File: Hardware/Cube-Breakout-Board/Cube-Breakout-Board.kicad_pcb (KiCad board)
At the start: 2 copper layers, 4 parts, among them J1 Conn_01x22, J2 Conn_01x30, J3 Pixhawk_Cube_DF17_80_Pin_Grou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, J4 Conn_01x30

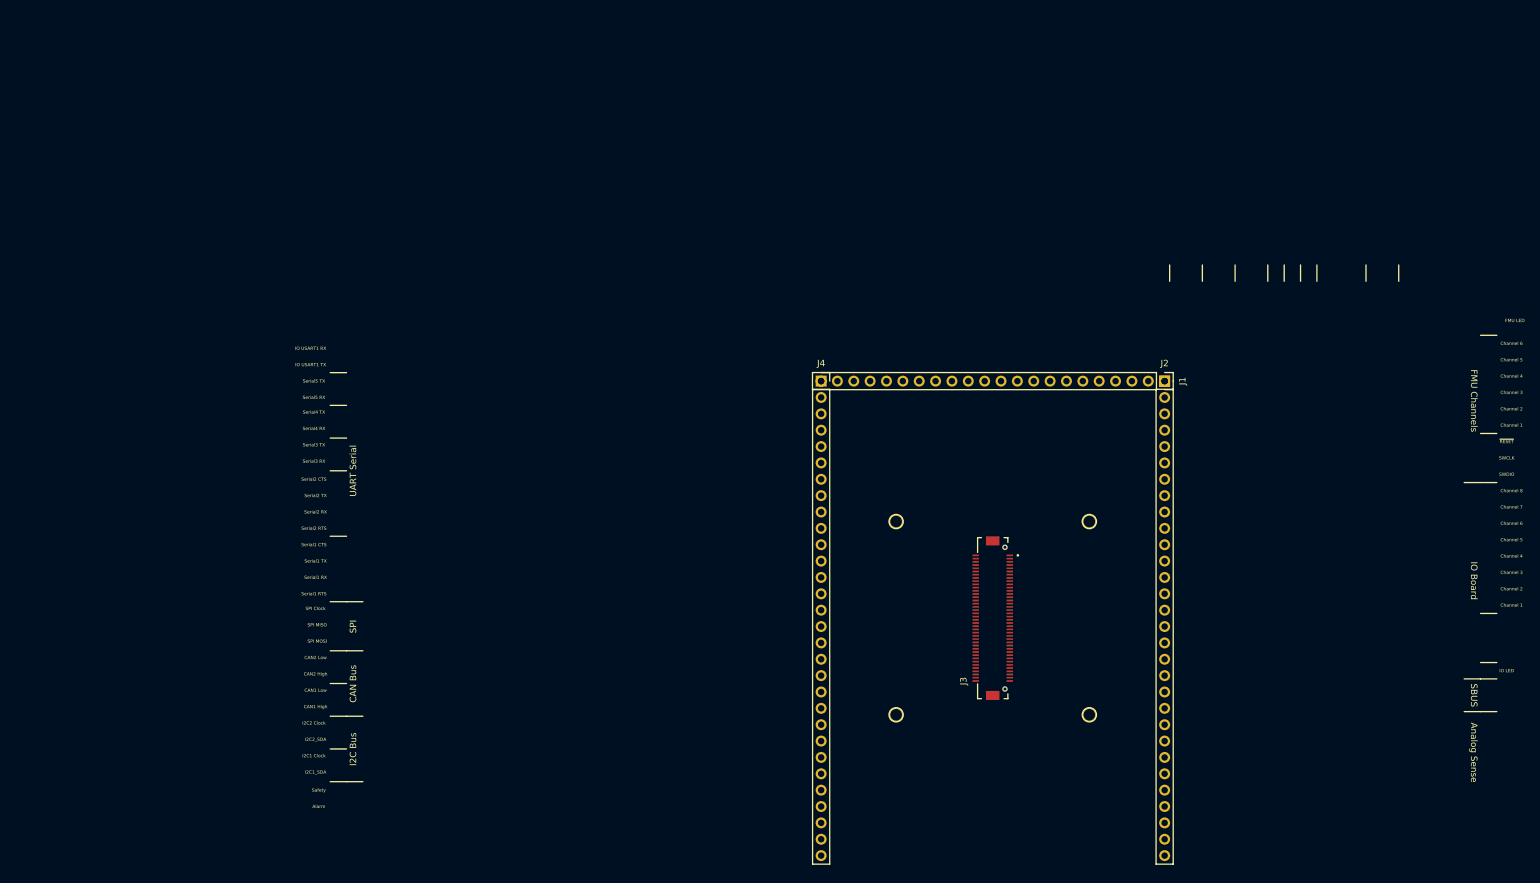
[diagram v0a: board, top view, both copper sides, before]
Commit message: Finished routing, board sizing, silkscreen text
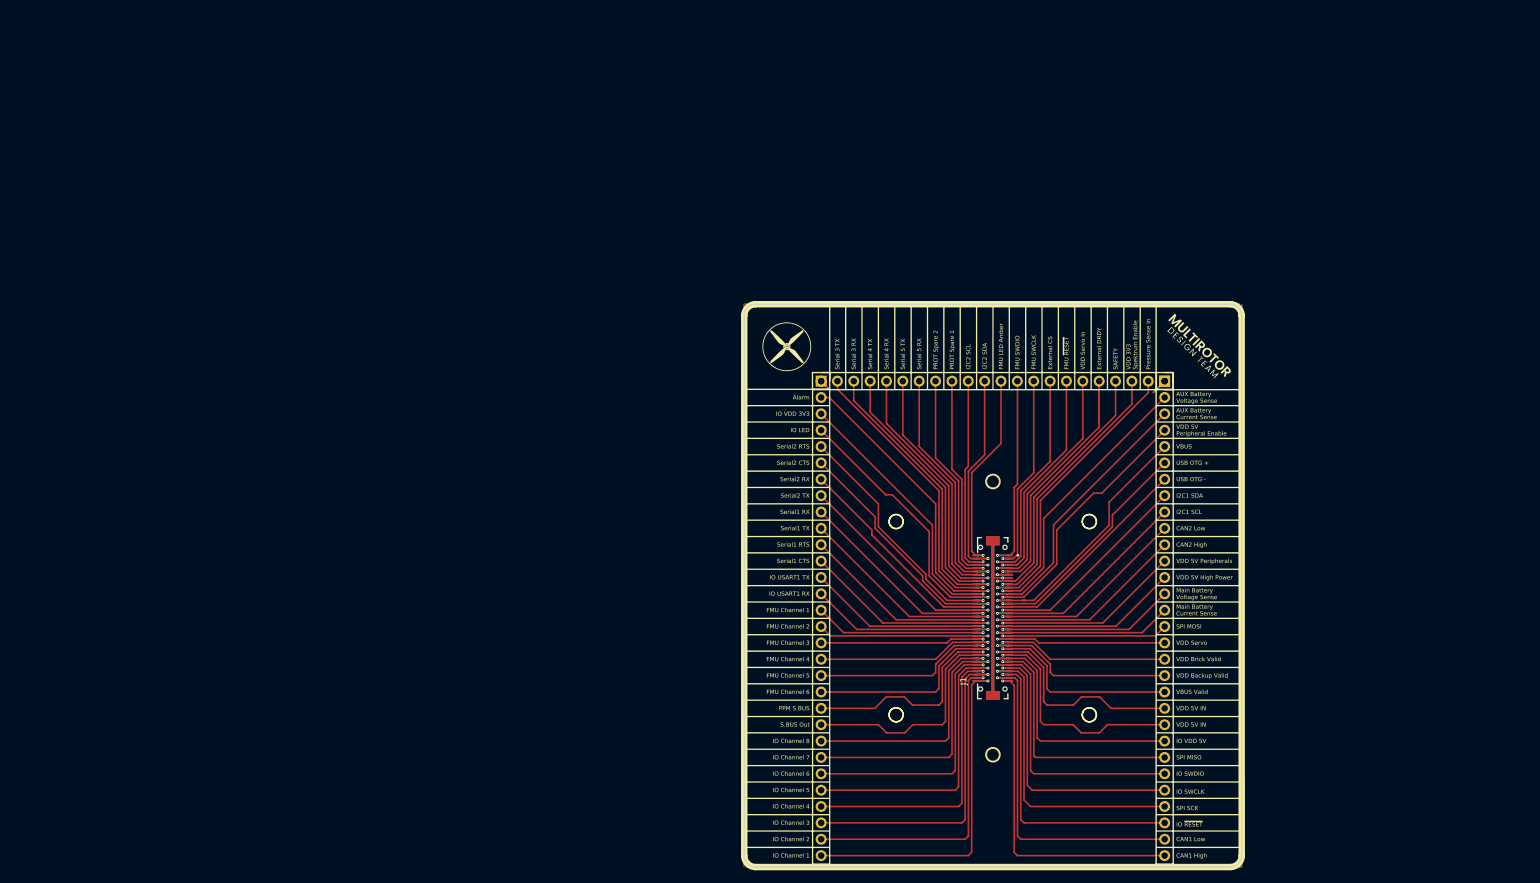
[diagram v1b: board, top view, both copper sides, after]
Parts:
- added ?: , clipboard:d1fccd29-87df-4368-b673-df9ed64eb982, F.Cu at (207.0, 132.8)
- added ?: , clipboard:d1fccd29-87df-4368-b673-df9ed64eb982, F.Cu at (207.0, 90.4)
- added G***: LOGO, libraries:MRR Logo Text, F.Cu at (238.7, 70.9)
- added G***: LOGO, libraries:MRR Logo 1, F.Cu at (175.0, 71.8)
- added J2: Pixhawk_Cube_DF17_80_Pin_Grouped, libraries:Cube_DF17_Mount, B.Cu at (207.0, 112.7)
- renumbered J3 to J1, J4 to J3, J1 to J4, J2 to J5
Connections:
- J1 pad 81: (no net) -> GND
- J1 pad S1: (no net) -> GND
- J1 pad S2: (no net) -> GND
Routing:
- net /VDD_5V_IN_PROT: track 0.00 -> 72.2 mm, vias 0 -> 2
- net GND: track 0.00 -> 65.0 mm, vias 0 -> 2
- net /IO_CH1_PROT: track 0.00 -> 54.3 mm, vias 0 -> 1
- net /CAN_H_1: track 0.00 -> 52.6 mm, vias 0 -> 1
- net /CAN_L_1: track 0.00 -> 52.4 mm, vias 0 -> 1
- net /IO_CH2_PROT: track 0.00 -> 50.8 mm, vias 0 -> 1
- net /IO_CH3_PROT: track 0.00 -> 50.2 mm, vias 0 -> 1
- net /IO_~{RESET}: track 0.00 -> 48.6 mm, vias 0 -> 1
- net /SPI_EXT_SCK: track 0.00 -> 47.8 mm, vias 0 -> 1
- net /ALARM: track 0.00 -> 46.5 mm, vias 0 -> 1
- net /IO_CH4_PROT: track 0.00 -> 46.5 mm, vias 0 -> 1
- net /IO_CH5_PROT: track 0.00 -> 45.8 mm, vias 0 -> 1
- net /PRESSURE_SENS_IN: track 0.00 -> 45.6 mm, vias 0 -> 1
- net /SERIAL_3_TX: track 0.00 -> 45.1 mm, vias 0 -> 1
- net /EXTERN_DRDY: track 0.00 -> 45.1 mm, vias 0 -> 1
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- added copper zone on B.Cu, net GND
- added copper zone on F.Cu, net GND
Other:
- board outline added: 77.2 x 87.4 mm
- board text added: "AUX Battery Current Sense"
- board text added: "AUX Battery Voltage Sense"
- board text added: "External CS"
- board text added: "External DRDY"
- board text added: "FMU Channel 1"
- board text added: "FMU Channel 2"
- board text added: "FMU Channel 3"
- board text added: "FMU Channel 4"
- board text added: "FMU Channel 5"
- board text added: "FMU Channel 6"
- board text added: "FMU LED Amber"
- board text added: "FMU SWCLK"
- board text added: "FMU SWDIO"
- board text added: "FMU ~{RESET}"
- board text added: "GND"
- board text added: "I2C1 SCL"
- board text added: "I2C1 SDA"
- board text added: "I2C2 SCL"
- board text added: "I2C2 SDA"
- board text added: "IO Channel 1"
- board text added: "IO Channel 2"
- board text added: "IO Channel 3"
- board text added: "IO Channel 4"
- board text added: "IO Channel 5"
- board text added: "IO Channel 6"
- board text added: "IO Channel 7"
- board text added: "IO Channel 8"
- board text added: "IO SWCLK"
- board text added: "IO SWDIO"
- board text added: "IO VDD 3V3"
- board text added: "IO VDD 5V"
- board text added: "IO ~{RESET}"
- board text added: "Main Battery Current Sense"
- board text added: "Main Battery Voltage Sense"
- board text added: "PPM S.BUS"
- board text added: "PROT Spare 1"
- board text added: "PROT Spare 2"
- board text added: "Pressure Sense In"
- board text added: "S.BUS Out"
- board text added: "SAFETY"
- board text added: "SPI SCK"
- board text added: "Serial 3 RX"
- board text added: "Serial 3 TX"
- board text added: "Serial 4 RX"
- board text added: "Serial 4 TX"
- board text added: "Serial 5 RX"
- board text added: "Serial 5 TX"
- board text added: "USB OTG +"
- board text added: "USB OTG -"
- board text added: "VBUS"
- board text added: "VBUS Valid"
- board text added: "VDD 3V3 Spektrum Enable"
- board text added: "VDD 5V High Power"
- board text added: "VDD 5V IN"
- board text added: "VDD 5V Peripheral Enable"
- board text added: "VDD 5V Peripherals"
- board text added: "VDD Backup Valid"
- board text added: "VDD Brick Valid"
- board text added: "VDD Servo"
- board text added: "VDD Servo In"
- board text removed: "Analog Sense"
- board text removed: "CAN Bus"
- board text removed: "Channel 1"
- board text removed: "Channel 2"
- board text removed: "Channel 3"
- board text removed: "Channel 4"
- board text removed: "Channel 5"
- board text removed: "Channel 6"
- board text removed: "Channel 7"
- board text removed: "Channel 8"
- board text removed: "FMU Channels"
- board text removed: "FMU LED"
- board text removed: "I2C Bus"
- board text removed: "I2C1 Clock"
- board text removed: "I2C1_SDA"
- board text removed: "I2C2 Clock"
- board text removed: "I2C2_SDA"
- board text removed: "IO Board"
- board text removed: "SBUS"
- board text removed: "SPI"
- board text removed: "SPI Clock"
- board text removed: "SWCLK"
- board text removed: "SWDIO"
- board text removed: "Safety"
- board text removed: "Serial3 RX"
- board text removed: "Serial3 TX"
- board text removed: "Serial4 RX"
- board text removed: "Serial4 TX"
- board text removed: "Serial5 RX"
- board text removed: "Serial5 TX"
- board text removed: "UART Serial"
- board text removed: "~{RESET}"

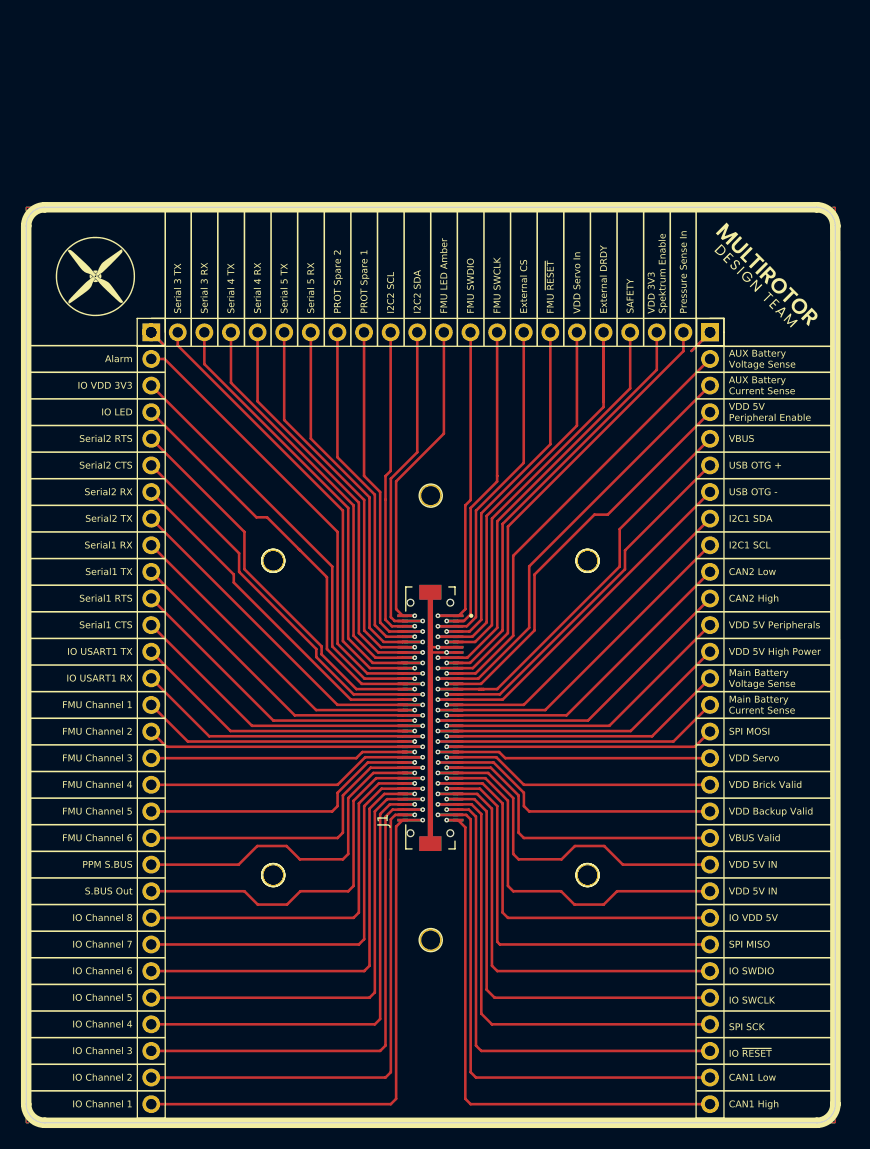
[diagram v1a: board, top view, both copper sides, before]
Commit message: Expanded layout to fit breadboards
Need to trim off 3mm of the height to meet max size for JLCPCB
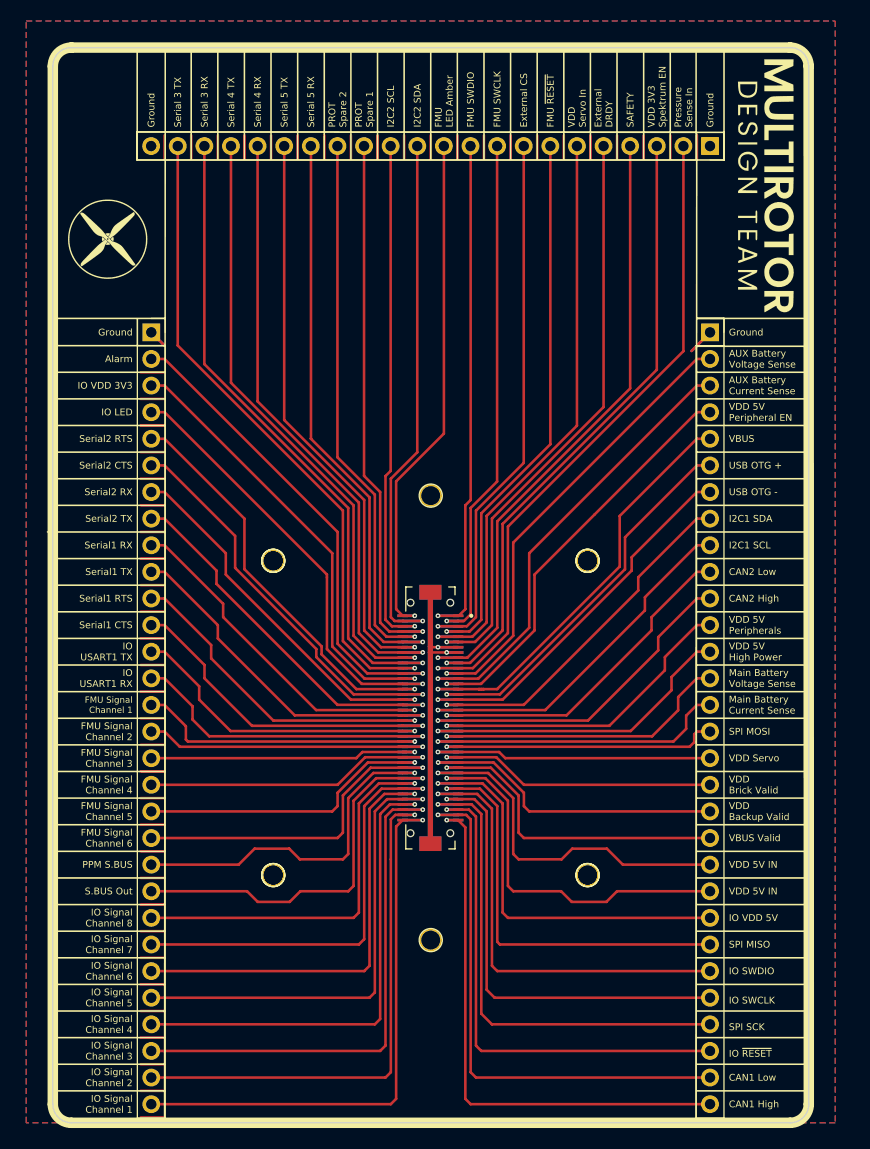
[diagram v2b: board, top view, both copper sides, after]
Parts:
- moved J4 17.8 mm to (233.7, 58.2)
- moved G*** 8.93 mm to (239.0, 61.9), turned to -90 degrees
- moved G*** 3.74 mm to (176.2, 68.2)
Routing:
- net GND: track 65.0 -> 179.5 mm
- net /SERIAL_4_RX: track 41.5 -> 59.3 mm
- net /I2C_2_SCL: track 31.8 -> 49.6 mm
- net /VDD_SERVO_IN: track 38.4 -> 56.2 mm
- net /VDD_3V3_SPEKTRUM_EN: track 42.3 -> 60.0 mm
- net /SERIAL_5_TX: track 38.3 -> 56.0 mm
- net /SERIAL_5_RX: track 38.1 -> 55.9 mm
- net /SERIAL_4_TX: track 41.7 -> 59.4 mm
- net /SERIAL_3_TX: track 45.1 -> 62.9 mm
- net /PRESSURE_SENS_IN: track 45.6 -> 63.4 mm
- net /I2C_2_SDA: track 33.3 -> 51.1 mm
- net /FMU_~{RESET}: track 35.0 -> 52.8 mm
- net /FMU_SWDIO: track 31.4 -> 49.2 mm
- net /FMU_LED_AMBER: track 31.5 -> 49.3 mm
- net /SERIAL_3_RX: track 44.9 -> 62.7 mm
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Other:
- board size 77.2 x 87.4 mm -> 72.1 x 102.6 mm
- board text added: "FMU Signal Channel 1"
- board text added: "FMU Signal Channel 2"
- board text added: "FMU Signal Channel 3"
- board text added: "FMU Signal Channel 4"
- board text added: "FMU Signal Channel 5"
- board text added: "FMU Signal Channel 6"
- board text added: "Ground"
- board text added: "IO Signal Channel 1"
- board text added: "IO Signal Channel 2"
- board text added: "IO Signal Channel 3"
- board text added: "IO Signal Channel 4"
- board text added: "IO Signal Channel 5"
- board text added: "IO Signal Channel 6"
- board text added: "IO Signal Channel 7"
- board text added: "IO Signal Channel 8"
- board text added: "VDD 3V3 Spektrum EN"
- board text added: "VDD 5V Peripheral EN"
- board text removed: "FMU Channel 1"
- board text removed: "FMU Channel 2"
- board text removed: "FMU Channel 3"
- board text removed: "FMU Channel 4"
- board text removed: "FMU Channel 5"
- board text removed: "FMU Channel 6"
- board text removed: "IO Channel 1"
- board text removed: "IO Channel 2"
- board text removed: "IO Channel 3"
- board text removed: "IO Channel 4"
- board text removed: "IO Channel 5"
- board text removed: "IO Channel 6"
- board text removed: "IO Channel 7"
- board text removed: "IO Channel 8"
- board text removed: "VDD 3V3 Spektrum Enable"
- board text removed: "VDD 5V Peripheral Enable"
